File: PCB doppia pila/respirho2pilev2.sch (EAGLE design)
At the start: 26 parts, among them U1 ICM-20948, U3 ADP1606ACPZN1.8-R7CP_6_3_ADI-L, X2 32.768kHz

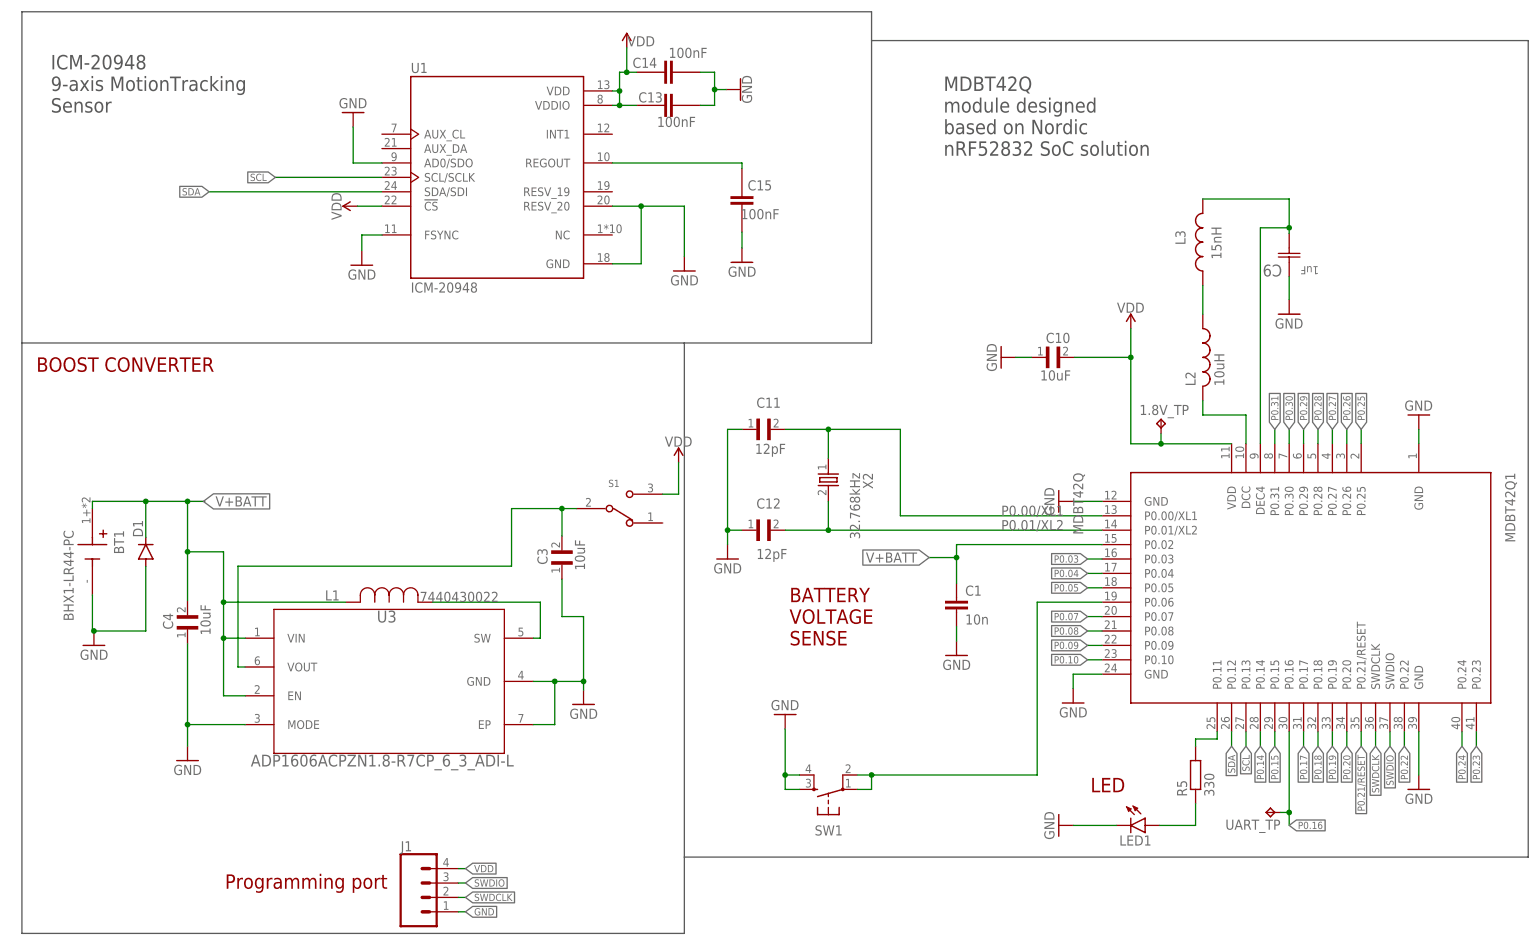
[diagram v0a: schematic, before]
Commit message: Aggiunte versioni con 2 pile
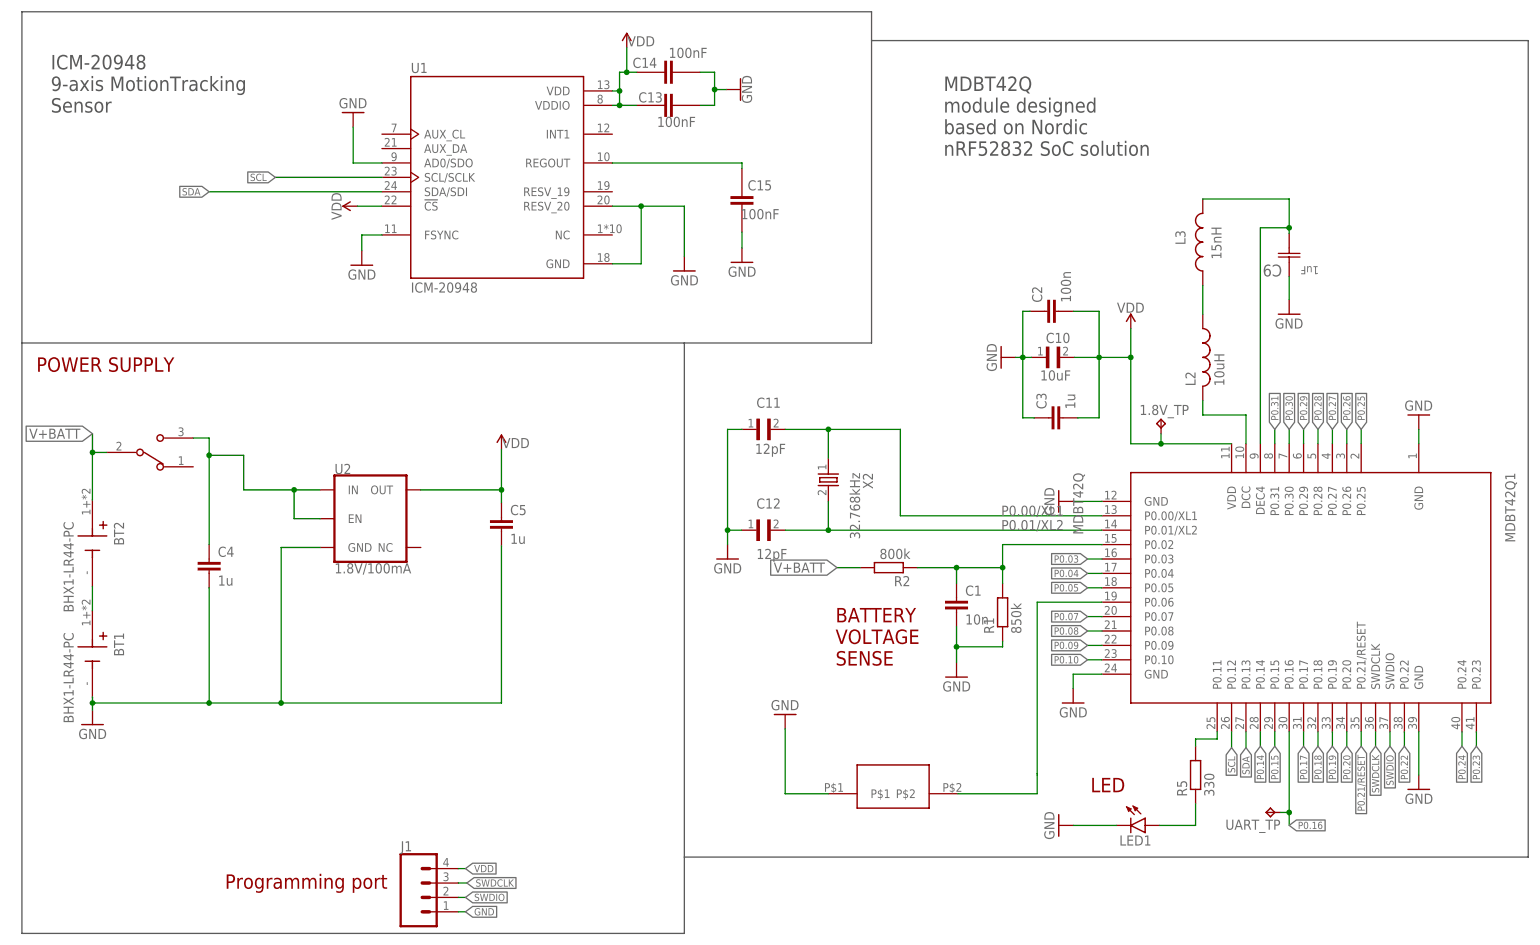
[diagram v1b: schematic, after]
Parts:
- removed D1: (no value), diode:DIODE-SOD323-R
- removed L1: 7440430022, inductor:7440430022
- removed S1: JS102011SAQN, JS102011SAQN:JS102011SAQN
- removed SW1: (no value), SparkFun-Electromechanical:SWITCH_SPST_4_PINRECT
- removed U3: ADP1606ACPZN1.8-R7CP_6_3_ADI-L, AD1606:ADP1606ACPZN1.8-R7CP_6_3_ADI-L
- added BT2: BHX1-LR44-PC, BHX1-LR44-PC:BHX1-LR44-PC
- added C2: 100n, rcl:C-EUC0402
- added C5: 1u, rcl:C-EUC0402
- added R1: 850k, rcl:R-EU_R0603
- added R2: 800k, rcl:R-EU_R0603
- added S2: EG1213, Slide_switch:EG1213
- added U$1: KSS231GLFS, KSS231GLFS:KSS231GLFS
- added U2: 1.8V/100mA, SparkFun-IC-Power:V_REG_SP6214-1.8V
- C3: value 10uF -> 1u; device GRM188R61A106KE69J:GRM188R61A106KE69J -> rcl:C-EUC0603
- C4: value 10uF -> 1u; device GRM188R61A106KE69J:GRM188R61A106KE69J -> rcl:C-EUC0402
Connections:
- removed net IND: L1.1, U3.SW
- removed net VOUT: C3.2, S1.2, U3.VOUT
- new net N$6: BT1.+, BT2.-
- new net N$8: C4.1, S2.3, U2.EN, U2.IN
- new net N$9: C1.1, MDBT42Q1.P0.02, R1.2, R2.1
- net GND: now also C2.1, C4.2, C5.2, R1.1, U$1.P$1, U2.GND; no longer C4.1, D1.A, SW1.3, SW1.4, U3.EP, U3.GND, U3.MODE
- net P06: now also U$1.P$2; no longer SW1.1, SW1.2
- net SCL: now also MDBT42Q1.P0.12; no longer MDBT42Q1.P0.13
- net SDA: now also MDBT42Q1.P0.13; no longer MDBT42Q1.P0.12
- net SWDCLK: now also J1.3; no longer J1.2
- net SWDIO: now also J1.2; no longer J1.3
- net V+BATT: now also BT2.+, R2.2, S2.2; no longer BT1.+, C1.1, C4.2, D1.C, L1.2, MDBT42Q1.P0.02, U3.EN, U3.VIN
- net VDD: now also C2.2, C3.2, C5.1, U2.OUT; no longer S1.3
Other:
- note added: "POWER SUPPLY"
- note removed: "BOOST CONVERTER"
- moved on the sheet: BT1, C3, C4
